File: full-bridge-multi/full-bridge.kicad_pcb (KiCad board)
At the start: 2 copper layers, 98.6 x 98.6 mm, 46 parts, among them J1 NegBus, J10 Screw_Terminal_01x02, J11 Bridge2, J12 Bridge1, J2 PosBus, J3 Conn_01x01, J4 Conn_01x01, J5 Conn_01x01, J6 Conn_01x01, J7 Screw_Terminal_01x02, J8 Screw_Terminal_01x02, J9 Screw_Terminal_01x02, Q1 Q_NIGBT_GCE, Q2 Q_NIGBT_GCE, Q3 Q_NIGBT_GCE, Q4 Q_NIGBT_GCE, Q5 Q_NIGBT_GCE, Q6 Q_NIGBT_GCE, Q7 Q_NIGBT_GCE, Q8 Q_NIGBT_GCE

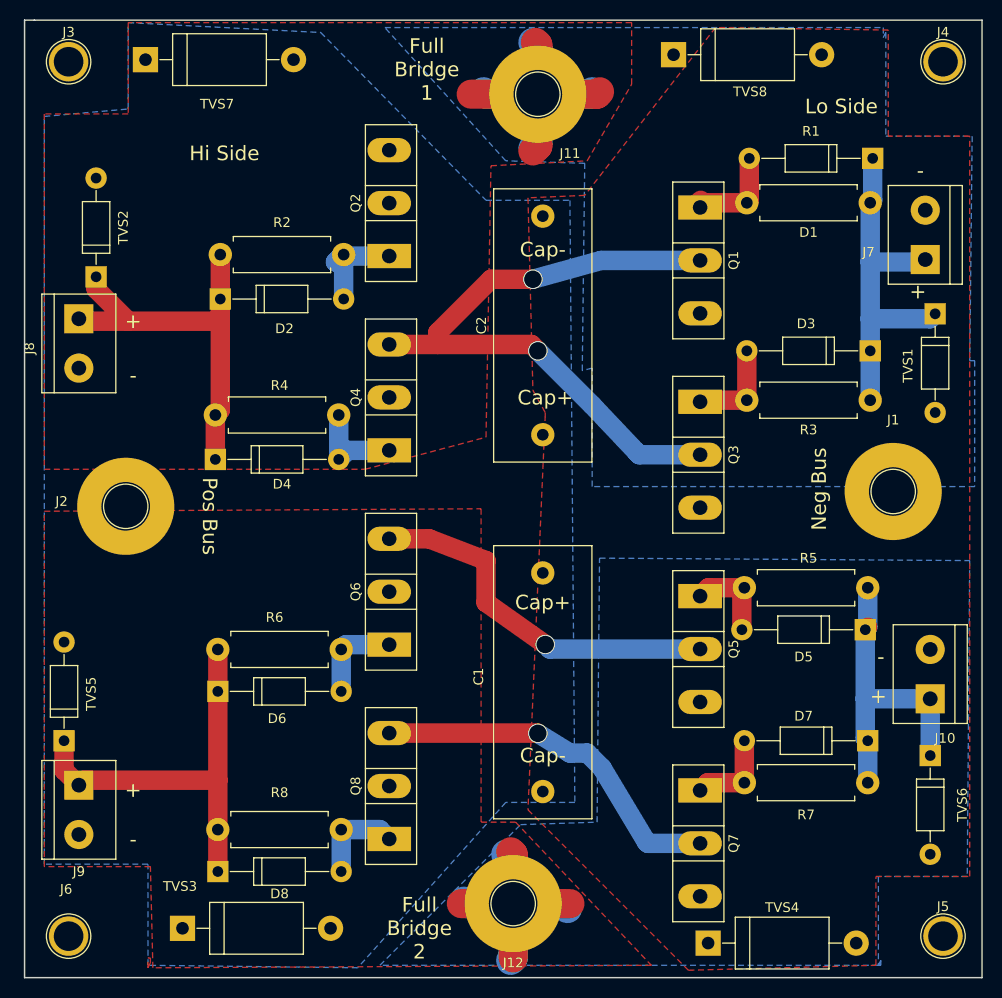
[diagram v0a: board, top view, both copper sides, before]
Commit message: Cleaned up labels and pads on half/full bridge boards
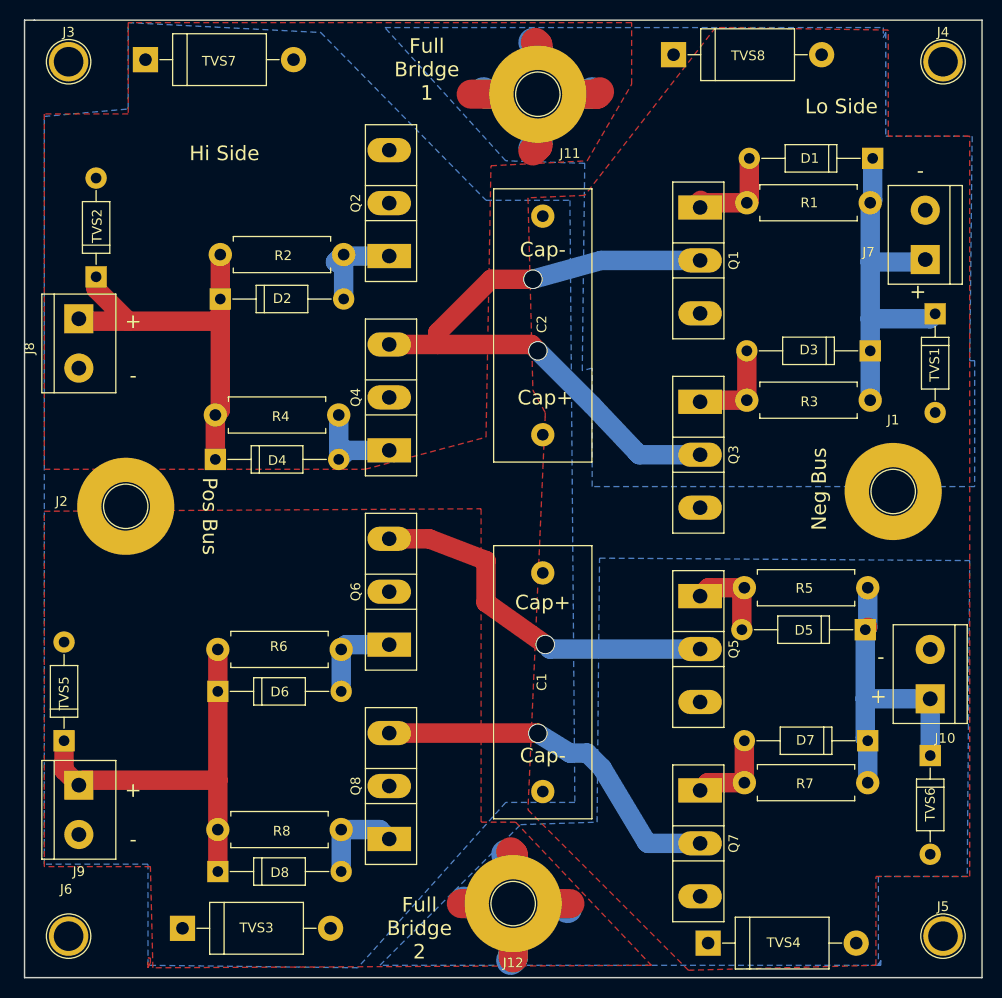
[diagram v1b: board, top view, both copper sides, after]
